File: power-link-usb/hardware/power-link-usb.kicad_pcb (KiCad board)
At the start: 4 copper layers, 50 x 34.5 mm, 30 parts, among them J1 KitProg3, J102 DX07S016JA3, J103 NE8FAH, J104 NE8FAH, Q101 BSC010N04LS, Q102 BSC010N04LS, U101 CYPM1311-48LDXI

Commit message: Update
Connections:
- net +VBUS renamed /+VBUS
- net +VLINK renamed /+VLINK
- net Shield renamed /Shield
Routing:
- net /USB+: track 30.1 -> 32.0 mm
- net /USB-: track 33.4 -> 34.1 mm
- net GND: vias 56 -> 60

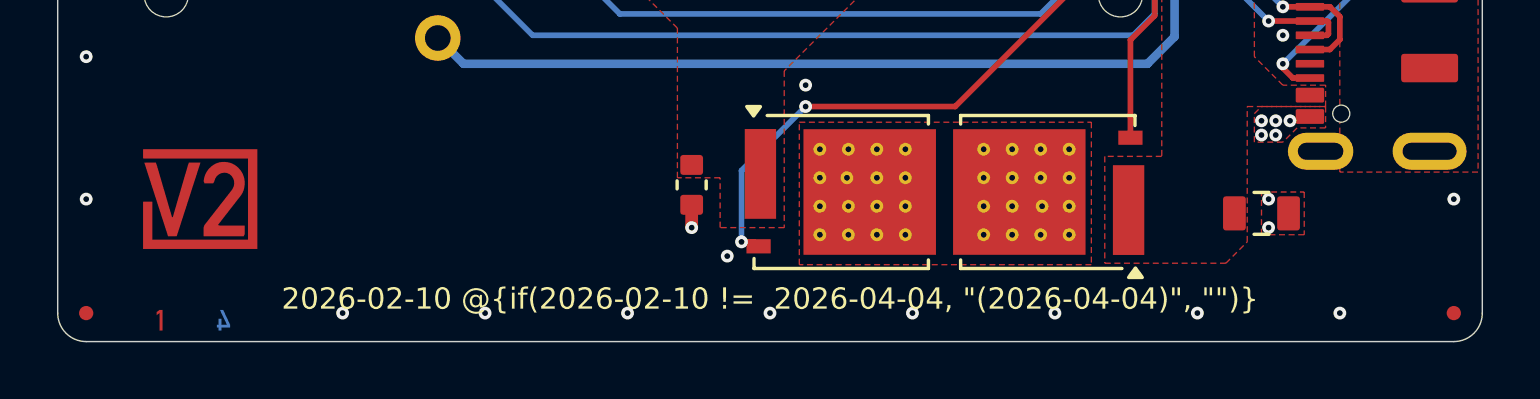
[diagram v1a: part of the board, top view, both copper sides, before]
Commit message: power-link-usb: split out PowerDelivery
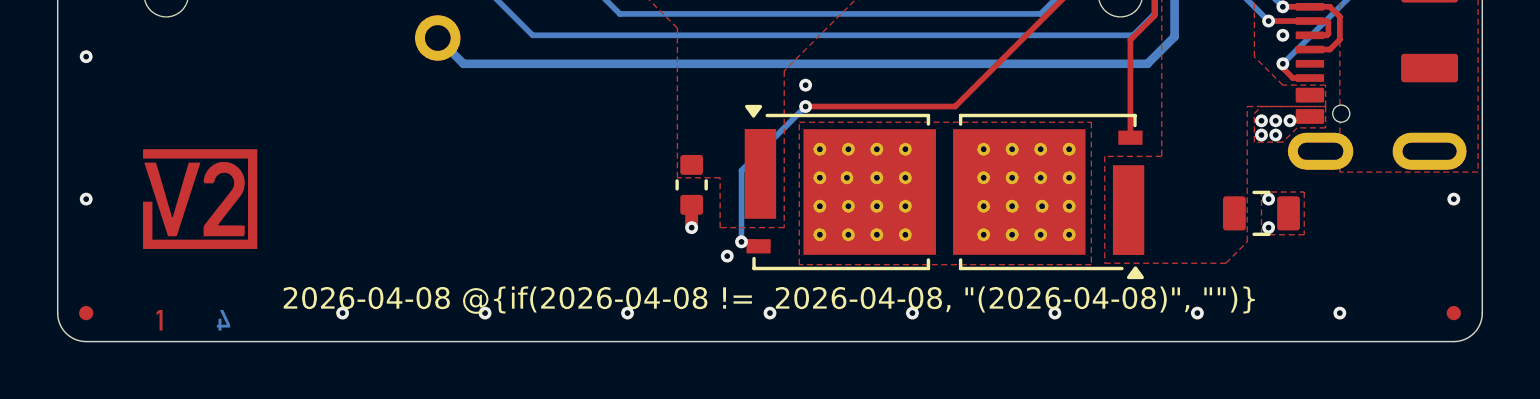
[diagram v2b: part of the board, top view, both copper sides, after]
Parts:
- renumbered C101 to C201, C102 to C202, C107 to C203, C103 to C204, C104 to C205, C108 to C206, C105 to C207, C106 to C208, D101 to D201, D102 to D202, J103 to J101, J104 to J102, J102 to J201, J1 to J202, Q101 to Q201, Q102 to Q202, R101 to R201, R102 to R202, R103 to R203, R104 to R204, R105 to R205, TVS101 to TVS201, TVS102 to TVS202, U101 to U201
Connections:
- net +3V3 renamed /PowerDelivery/+VSUPPLY
- net /+1V8 renamed /PowerDelivery/+VCORE
- net /+VBUS renamed /PowerDelivery/+VBUS
- net /Drain renamed /PowerDelivery/Drain
- net /LED-Orange renamed /PowerDelivery/LED-Orange
- net /LED-Red renamed /PowerDelivery/LED-Red
- net /RESET renamed /PowerDelivery/RESET
- net /Rail-Input renamed /PowerDelivery/Rail-Input
- net /Rail-Output renamed /PowerDelivery/Rail-Output
- net /SCK renamed /PowerDelivery/SCL
- net /SDA renamed /PowerDelivery/SDA
- net /SWCLK renamed /PowerDelivery/SWCLK
- net /SWDIO renamed /PowerDelivery/SWDIO
- net /Shield renamed /PowerDelivery/Shield
- net /UART-RX renamed /PowerDelivery/UART-RX
- net /UART-TX renamed /PowerDelivery/UART-TX
- net /USB+ renamed /PowerDelivery/USB+
- net /USB- renamed /PowerDelivery/USB-
- net /USB-CC1 renamed /PowerDelivery/USB-CC1
- net /USB-CC2 renamed /PowerDelivery/USB-CC2

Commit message: Update
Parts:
- renumbered TVS202 to TVS101
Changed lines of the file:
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@@
 		(sheetname "/PowerDelivery/")
 		(sheetfile "PowerDelivery.kicad_sch")
+		(units
+			(unit
+				(name "A")
+				(pins "1" "2")
+			)
+		)
 		(attr smd)
 		(duplicate_pad_numbers_are_jumpers no)
@@
 		(sheetname "/PowerDelivery/")
 		(sheetfile "PowerDelivery.kicad_sch")
+		(units
+			(unit
+				(name "A")
+				(pins "1" "2")
+			)
+		)
 		(attr smd)
 		(duplicate_pad_numbers_are_jumpers no)
@@
 		(sheetname "/PowerDelivery/")
 		(sheetfile "PowerDelivery.kicad_sch")
+		(units
+			(unit
+				(name "A")
+				(pins "4" "5" "1")
+			)
+		)
 		(attr smd)
 		(duplicate_pad_numbers_are_jumpers no)
@@
 		(sheetname "/PowerDelivery/")
 		(sheetfile "PowerDelivery.kicad_sch")
+		(units
+			(unit
+				(name "A")
+				(pins "1" "2")
+			)
+		)
 		(attr smd)
 		(duplicate_pad_numbers_are_jumpers no)
@@
 		(sheetname "/PowerDelivery/")
 		(sheetfile "PowerDelivery.kicad_sch")
+		(units
+			(unit
+				(name "A")
+				(pins "1" "2")
+			)
+		)
 		(attr smd)
 		(duplicate_pad_numbers_are_jumpers no)
@@
 		(sheetname "/PowerDelivery/")
 		(sheetfile "PowerDelivery.kicad_sch")
+		(units
+			(unit
+				(name "A")
+				(pins "1" "2")
+			)
+		)
 		(attr smd)
 		(duplicate_pad_numbers_are_jumpers no)
@@
 		(sheetname "/PowerDelivery/")
 		(sheetfile "PowerDelivery.kicad_sch")
+		(units
+			(unit
+				(name "A")
+				(pins "S" "G" "V" "A5" "B5" "A7" "B7" "A6" "B6" "A8" "B8")
+			)
+		)
 		(duplicate_pad_numbers_are_jumpers no)
 		(fp_poly
@@
 		(sheetname "/PowerDelivery/")
 		(sheetfile "PowerDelivery.kicad_sch")
+		(units
+			(unit
+				(name "A")
+				(pins "1" "2")
+			)
+		)
 		(attr smd)
 		(duplicate_pad_numbers_are_jumpers no)
@@
 		(sheetname "/")
 		(sheetfile "power-link-usb.kicad_sch")
-		(attr exclude_from_pos_files exclude_from_bom allow_missing_courtyard)
+		(units
+			(unit
+				(name "A")
+				(pins)
+			)
+		)
+		(attr exclude_from_bom allow_missing_courtyard)
 		(duplicate_pad_numbers_are_jumpers no)
 		(fp_text user "${REVISION} @{if(${REVISION} !=  ${ISSUE_DATE}, \"(${ISSUE_DATE})\", \"\")}"
@@
 		(sheetname "/PowerDelivery/")
 		(sheetfile "PowerDelivery.kicad_sch")
+		(units
+			(unit
+				(name "A")
+				(pins "1" "2")
+			)
+		)
 		(attr smd)
 		(duplicate_pad_numbers_are_jumpers no)
@@
 		(sheetname "/PowerDelivery/")
 		(sheetfile "PowerDelivery.kicad_sch")
+		(units
+			(unit
+				(name "A")
+				(pins "1" "2" "3" "4" "5" "6" "7" "8" "9" "10" "11" "12" "48" "13" "47"
+					"14" "46" "15" "45" "16" "44" "17" "43" "18" "42" "19" "41" "20" "40"
+					"21" "39" "22" "38" "23" "37" "24" "49" "36" "35" "34" "33" "32" "31"
+					"30" "29" "28" "27" "26" "25"
+				)
+			)
+		)
 		(attr smd)
 		(duplicate_pad_numbers_are_jumpers no)
@@
 		(sheetname "/PowerDelivery/")
 		(sheetfile "PowerDelivery.kicad_sch")
+		(units
+			(unit
+				(name "A")
+				(pins "1" "2")
+			)
+		)
 		(attr smd)
 		(duplicate_pad_numbers_are_jumpers no)
@@
 		(sheetname "/PowerDelivery/")
 		(sheetfile "PowerDelivery.kicad_sch")
+		(units
+			(unit
+				(name "A")
+				(pins "1" "2")
+			)
+		)
 		(attr smd)
 		(duplicate_pad_numbers_are_jumpers no)
@@
 		(sheetname "/PowerDelivery/")
 		(sheetfile "PowerDelivery.kicad_sch")
-		(attr exclude_from_pos_files exclude_from_bom)
+		(units
+			(unit
+				(name "A")
+				(pins "4" "6" "8" "10" "1" "3" "5" "7" "9")
+			)
+		)
+		(attr exclude_from_bom)
 		(duplicate_pad_numbers_are_jumpers no)
 		(fp_line
@@
 		(descr "Diode SMB (DO-214AA)")
 		(tags "Diode SMB (DO-214AA)")
-		(property "Reference" "TVS202"
+		(property "Reference" "TVS101"
 			(at 0 -3 270)
 			(layer "F.SilkS")
@@
 			)
 		)
-		(sheetname "/PowerDelivery/")
-		(sheetfile "PowerDelivery.kicad_sch")
+		(sheetname "/")
+		(sheetfile "power-link-usb.kicad_sch")
+		(units
+			(unit
+				(name "A")
+				(pins "1" "2")
+			)
+		)
 		(attr smd)
 		(duplicate_pad_numbers_are_jumpers no)
@@
 		(sheetname "/PowerDelivery/")
 		(sheetfile "PowerDelivery.kicad_sch")
+		(units
+			(unit
+				(name "A")
+				(pins "4" "5" "1")
+			)
+		)
 		(attr smd)
 		(duplicate_pad_numbers_are_jumpers no)
@@
 		(sheetname "/")
 		(sheetfile "power-link-usb.kicad_sch")
-		(attr exclude_from_pos_files exclude_from_bom allow_missing_courtyard)
+		(units
+			(unit
+				(name "A")
+				(pins)
+			)
+		)
+		(attr exclude_from_bom allow_missing_courtyard)
 		(stackup
 			(layer "F.Cu")
@@
 		(sheetname "/PowerDelivery/")
 		(sheetfile "PowerDelivery.kicad_sch")
+		(units
+			(unit
+				(name "A")
+				(pins "1" "2")
+			)
+		)
 		(attr smd)
 		(duplicate_pad_numbers_are_jumpers no)
@@
 		(sheetname "/PowerDelivery/")
 		(sheetfile "PowerDelivery.kicad_sch")
+		(units
+			(unit
+				(name "A")
+				(pins "1" "2")
+			)
+		)
 		(attr smd)
 		(duplicate_pad_numbers_are_jumpers no)
@@
 		(sheetname "/PowerDelivery/")
 		(sheetfile "PowerDelivery.kicad_sch")
+		(units
+			(unit
+				(name "A")
+				(pins "1" "2")
+			)
+		)
 		(attr smd)
 		(duplicate_pad_numbers_are_jumpers no)
@@
 		(sheetname "/")
 		(sheetfile "power-link-usb.kicad_sch")
+		(units
+			(unit
+				(name "A")
+				(pins)
+			)
+		)
 		(attr exclude_from_bom)
 		(duplicate_pad_numbers_are_jumpers no)
@@
 		(sheetname "/PowerDelivery/")
 		(sheetfile "PowerDelivery.kicad_sch")
+		(units
+			(unit
+				(name "A")
+				(pins "1" "2")
+			)
+		)
 		(attr smd)
 		(duplicate_pad_numbers_are_jumpers no)
@@
 		(sheetname "/")
 		(sheetfile "power-link-usb.kicad_sch")
+		(units
+			(unit
+				(name "A")
+				(pins)
+			)
+		)
 		(attr exclude_from_bom)
 		(duplicate_pad_numbers_are_jumpers no)
@@
 		(sheetname "/PowerDelivery/")
 		(sheetfile "PowerDelivery.kicad_sch")
+		(units
+			(unit
+				(name "A")
+				(pins "1" "2")
+			)
+		)
 		(attr smd)
 		(duplicate_pad_numbers_are_jumpers no)
@@
 		(sheetname "/PowerDelivery/")
 		(sheetfile "PowerDelivery.kicad_sch")
+		(units
+			(unit
+				(name "A")
+				(pins "1" "2")
+			)
+		)
 		(attr smd)
 		(duplicate_pad_numbers_are_jumpers no)
@@
 		(sheetname "/")
 		(sheetfile "power-link-usb.kicad_sch")
+		(units
+			(unit
+				(name "A")
+				(pins)
+			)
+		)
 		(attr exclude_from_bom)
 		(duplicate_pad_numbers_are_jumpers no)
@@
 		(sheetname "/PowerDelivery/")
 		(sheetfile "PowerDelivery.kicad_sch")
+		(units
+			(unit
+				(name "A")
+				(pins "1" "2")
+			)
+		)
 		(attr smd)
 		(duplicate_pad_numbers_are_jumpers no)
@@
 		(sheetname "/")
 		(sheetfile "power-link-usb.kicad_sch")
-		(attr exclude_from_pos_files exclude_from_bom allow_missing_courtyard)
+		(units
+			(unit
+				(name "A")
+				(pins)
+			)
+		)
+		(attr exclude_from_bom allow_missing_courtyard)
 		(duplicate_pad_numbers_are_jumpers no)
 		(fp_poly
@@
 		(sheetname "/")
 		(sheetfile "power-link-usb.kicad_sch")
+		(units
+			(unit
+				(name "A")
+				(pins "S" "8" "7" "6" "5" "4" "3" "2" "1")
+			)
+		)
 		(attr through_hole allow_missing_courtyard)
 		(duplicate_pad_numbers_are_jumpers no)
@@
 		(sheetname "/")
 		(sheetfile "power-link-usb.kicad_sch")
+		(units
+			(unit
+				(name "A")
+				(pins "S" "8" "7" "6" "5" "4" "3" "2" "1")
+			)
+		)
 		(attr through_hole allow_missing_courtyard)
 		(duplicate_pad_numbers_are_jumpers no)
